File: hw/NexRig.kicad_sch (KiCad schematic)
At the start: 7 parts

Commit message: Giant rename to actual NexRig project name which seems to have stuck
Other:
- sheet Power ports: added none; removed FPGA1V2enable
- sheet microcontroller ports: added none; removed FPGA1V2enable
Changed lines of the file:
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@@
 			"qsdPh1d" "qsdPh2a" "qsdPh2b" "qsdPh2c" "qsdPh2d" "bruene" "txData" "txBCLK"
 			"txMCLK" "txWCLK" "usbReset" "usbPOK2" "usbPOK3" "usbnALERT" "enable6V"
-			"enFPGASPIVdd" "enFPGAVpp" "nTxRelay" "enFPGAIOVdd" "audioSCL" "audioSDA"
+			"enable3VA" "enable5VA" "nTxRelay" "enable3V3" "audioSCL" "audioSDA" "enableFPGA1V2"
+			"enableFPGAIO"
 		)
 	)
@@
 		)
 	)
-	(wire
-		(pts
-			(xy 173.99 99.06) (xy 189.23 99.06)
-		)
-		(stroke
-			(width 0)
-			(type default)
-		)
-	)
 	(symbol
 		(lib_id "Mechanical:Fiducial")
@@
 		)
 		(instances
-			(project "USB-SSB-txcvr"
+			(project "NexRig"
 				(path "/8ae46c04-d01a-4756-8774-512b694bfaff"
 					(reference "FID102")
@@
 		)
 		(instances
-			(project "USB-SSB-txcvr"
+			(project "NexRig"
 				(path "/8ae46c04-d01a-4756-8774-512b694bfaff"
 					(reference "FID103")
@@
 		)
 		(instances
-			(project "USB-SSB-txcvr"
+			(project "NexRig"
 				(path "/8ae46c04-d01a-4756-8774-512b694bfaff"
 					(reference "#PWR0103")
@@
 		)
 		(instances
-			(project "USB-SSB-txcvr"
+			(project "NexRig"
 				(path "/8ae46c04-d01a-4756-8774-512b694bfaff"
 					(reference "#PWR0102")
@@
 		)
 		(instances
-			(project "USB-SSB-txcvr"
+			(project "NexRig"
 				(path "/8ae46c04-d01a-4756-8774-512b694bfaff"
 					(reference "#PWR0104")
@@
 		)
 		(instances
-			(project "USB-SSB-txcvr"
+			(project "NexRig"
 				(path "/8ae46c04-d01a-4756-8774-512b694bfaff"
 					(reference "MH102")
@@
 		)
 		(instances
-			(project "USB-SSB-txcvr"
+			(project "NexRig"
 				(path "/8ae46c04-d01a-4756-8774-512b694bfaff"
 					(reference "MH103")
@@
 		)
 		(instances
-			(project "USB-SSB-txcvr"
+			(project "NexRig"
 				(path "/8ae46c04-d01a-4756-8774-512b694bfaff"
 					(reference "MH104")
@@
 		)
 		(instances
-			(project "USB-SSB-txcvr"
+			(project "NexRig"
 				(path "/8ae46c04-d01a-4756-8774-512b694bfaff"
 					(page "3")
@@
 		)
 		(instances
-			(project "USB-SSB-txcvr"
+			(project "NexRig"
 				(path "/8ae46c04-d01a-4756-8774-512b694bfaff"
 					(page "6")
@@
 		)
 		(instances
-			(project "USB-SSB-txcvr"
+			(project "NexRig"
 				(path "/8ae46c04-d01a-4756-8774-512b694bfaff"
 					(page "5")
@@
 			)
 		)
-		(pin "FPGA1V2enable" output
-			(at 189.23 99.06 180)
-			(effects
-				(font
-					(size 1.27 1.27)
-				)
-				(justify left)
-			)
-		)
 		(pin "scaledEERVdd" input
 			(at 189.23 101.6 180)
@@
 		)
 		(instances
-			(project "USB-SSB-txcvr"
+			(project "NexRig"
 				(path "/8ae46c04-d01a-4756-8774-512b694bfaff"
 					(page "2")
@@
 			)
 		)
-		(pin "FPGA1V2enable" input
-			(at 173.99 99.06 0)
-			(effects
-				(font
-					(size 1.27 1.27)
-				)
-				(justify right)
-			)
-		)
 		(pin "scaledEERVdd" output
 			(at 173.99 101.6 0)
@@
 		)
 		(instances
-			(project "USB-SSB-txcvr"
+			(project "NexRig"
 				(path "/8ae46c04-d01a-4756-8774-512b694bfaff"
 					(page "18")

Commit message: Schematic capture of the USBPD and +12V (+12V has priority) power scheme is "done". Have started working on RF deck mezzanine module but not yet divorced into another project
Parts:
- renumbered FID101 to FID7701, FID102 to FID7702, FID103 to FID7703, MH101 to MH7701, MH102 to MH7702, MH103 to MH7703, MH104 to MH7704
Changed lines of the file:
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@@
 		(dnp no)
 		(fields_autoplaced yes)
-		(property "Reference" "FID102"
+		(property "Reference" "FID7702"
 			(at 69.85 180.3399 0)
 			(effects
@@
 			(project "NexRig"
 				(path "/8ae46c04-d01a-4756-8774-512b694bfaff"
-					(reference "FID102")
+					(reference "FID7702")
 					(unit 1)
 				)
@@
 		(dnp no)
 		(fields_autoplaced yes)
-		(property "Reference" "FID103"
+		(property "Reference" "FID7703"
 			(at 86.36 180.3399 0)
 			(effects
@@
 			(project "NexRig"
 				(path "/8ae46c04-d01a-4756-8774-512b694bfaff"
-					(reference "FID103")
+					(reference "FID7703")
 					(unit 1)
 				)
@@
 		(dnp no)
 		(fields_autoplaced yes)
-		(property "Reference" "FID101"
+		(property "Reference" "FID7701"
 			(at 52.07 180.3399 0)
 			(effects
@@
 			(project ""
 				(path "/8ae46c04-d01a-4756-8774-512b694bfaff"
-					(reference "FID101")
+					(reference "FID7701")
 					(unit 1)
 				)
@@
 		(dnp no)
 		(fields_autoplaced yes)
-		(property "Reference" "MH101"
+		(property "Reference" "MH7701"
 			(at 36.83 158.7499 0)
 			(effects
@@
 			(project ""
 				(path "/8ae46c04-d01a-4756-8774-512b694bfaff"
-					(reference "MH101")
+					(reference "MH7701")
 					(unit 1)
 				)
@@
 		(dnp no)
 		(fields_autoplaced yes)
-		(property "Reference" "#PWR0103"
+		(property "Reference" "#PWR07703"
 			(at 73.66 171.45 0)
 			(effects
@@
 			(project "NexRig"
 				(path "/8ae46c04-d01a-4756-8774-512b694bfaff"
-					(reference "#PWR0103")
+					(reference "#PWR07703")
 					(unit 1)
 				)
@@
 		(dnp no)
 		(fields_autoplaced yes)
-		(property "Reference" "#PWR0102"
+		(property "Reference" "#PWR07702"
 			(at 53.34 171.45 0)
 			(effects
@@
 			(project "NexRig"
 				(path "/8ae46c04-d01a-4756-8774-512b694bfaff"
-					(reference "#PWR0102")
+					(reference "#PWR07702")
 					(unit 1)
 				)
@@
 		(dnp no)
 		(fields_autoplaced yes)
-		(property "Reference" "#PWR0104"
+		(property "Reference" "#PWR07704"
 			(at 93.98 171.45 0)
 			(effects
@@
 			(project "NexRig"
 				(path "/8ae46c04-d01a-4756-8774-512b694bfaff"
-					(reference "#PWR0104")
+					(reference "#PWR07704")
 					(unit 1)
 				)
@@
 		(dnp no)
 		(fields_autoplaced yes)
-		(property "Reference" "MH102"
+		(property "Reference" "MH7702"
 			(at 55.88 158.7499 0)
 			(effects
@@
 			(project "NexRig"
 				(path "/8ae46c04-d01a-4756-8774-512b694bfaff"
-					(reference "MH102")
+					(reference "MH7702")
 					(unit 1)
 				)
@@
 		(dnp no)
 		(fields_autoplaced yes)
-		(property "Reference" "MH103"
+		(property "Reference" "MH7703"
 			(at 76.2 158.7499 0)
 			(effects
@@
 			(project "NexRig"
 				(path "/8ae46c04-d01a-4756-8774-512b694bfaff"
-					(reference "MH103")
+					(reference "MH7703")
 					(unit 1)
 				)
@@
 		(dnp no)
 		(fields_autoplaced yes)
-		(property "Reference" "#PWR0101"
+		(property "Reference" "#PWR07701"
 			(at 34.29 171.45 0)
 			(effects
@@
 			(project ""
 				(path "/8ae46c04-d01a-4756-8774-512b694bfaff"
-					(reference "#PWR0101")
+					(reference "#PWR07701")
 					(unit 1)
 				)
@@
 		(dnp no)
 		(fields_autoplaced yes)
-		(property "Reference" "MH104"
+		(property "Reference" "MH7704"
 			(at 96.52 158.7499 0)
 			(effects
@@
 			(project "NexRig"
 				(path "/8ae46c04-d01a-4756-8774-512b694bfaff"
-					(reference "MH104")
-					(unit 1)
-				)
+					(reference "MH7704")
+					(unit 1)
+				)

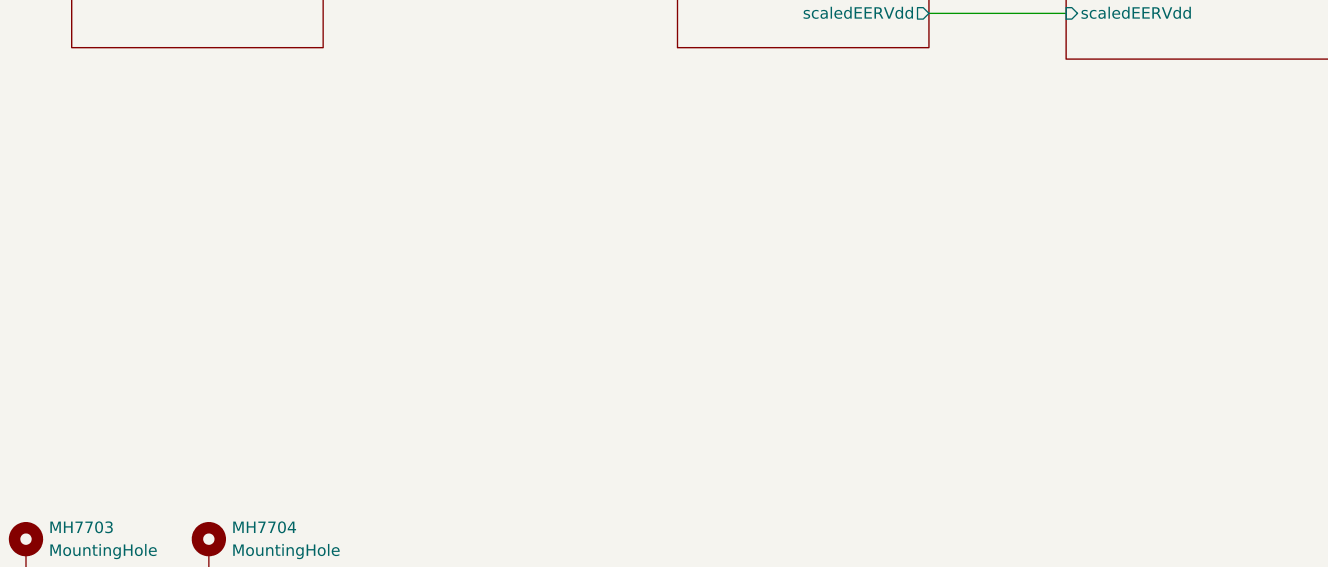
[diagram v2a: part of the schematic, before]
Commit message: Last rites for 800 ohm rx preselector, and probably the RF deck which was stillborn
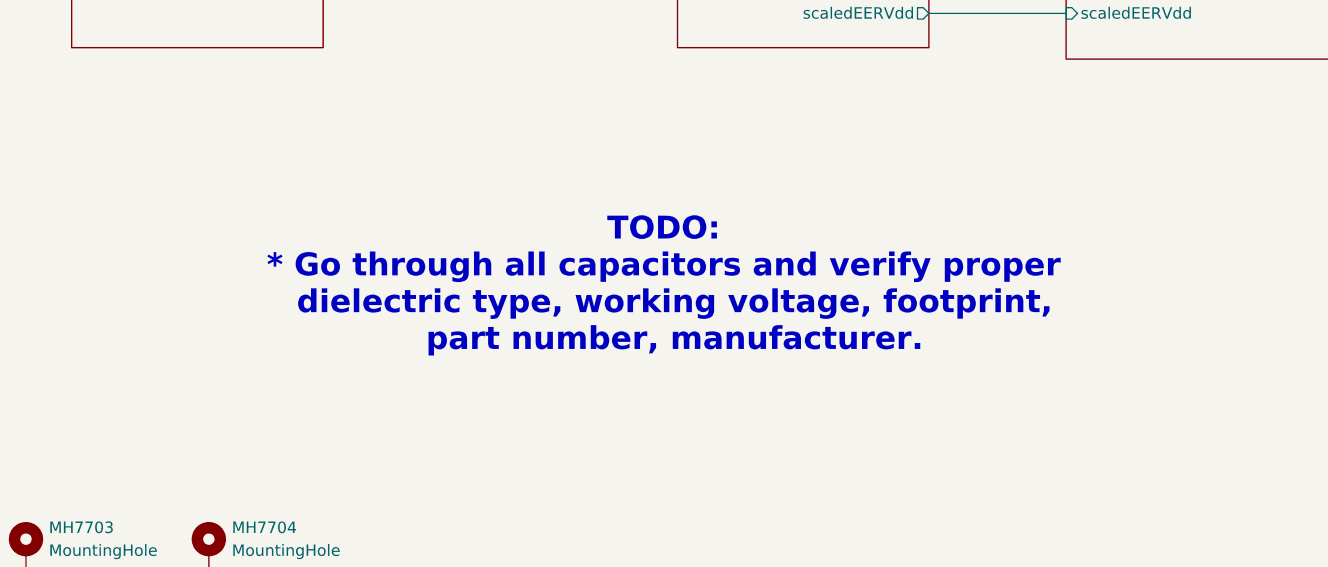
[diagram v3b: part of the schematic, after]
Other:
- note added: "TODO: * Go through all capacitors and verify proper dielectric type, working voltage, footprint, part number, manufacturer."
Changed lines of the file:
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@@
 	(title_block
 		(title "NexRig")
-		(date "2025-08-10")
+		(date "2025-10-13")
 		(company "WB7NAB")
 		(comment 1 "Alan Mimms")
@@
 		)
 	)
+	(text "TODO:\n* Go through all capacitors and verify proper\n  dielectric type, working voltage, footprint,\n  part number, manufacturer.\n"
+		(exclude_from_sim no)
+		(at 144.526 131.826 0)
+		(effects
+			(font
+				(size 2.54 2.54)
+				(thickness 0.508)
+				(bold yes)
+			)
+		)
+	)
